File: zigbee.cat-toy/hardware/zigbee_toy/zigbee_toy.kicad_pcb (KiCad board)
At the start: 2 copper layers, 36 x 23 mm, 71 parts, among them J1 USB-C 16P, J3 LiPo 1S (JST-PH), J4 MOTOR, J5 SPEAKER, Q1 AO3401A, Q2 AO3400A, SW1 PAIR / BOOT, U1 ESP32-C6-MINI-1U-H4, U2 DRV8213DSGR, U3 LIS2DW12TR-MS, U4 TP4054-42-SOT25R, U5 XB5353A, U6 RT9080-33GJ5, U7 USBLC6-2SC6, Y1 32.768k 12.5pF

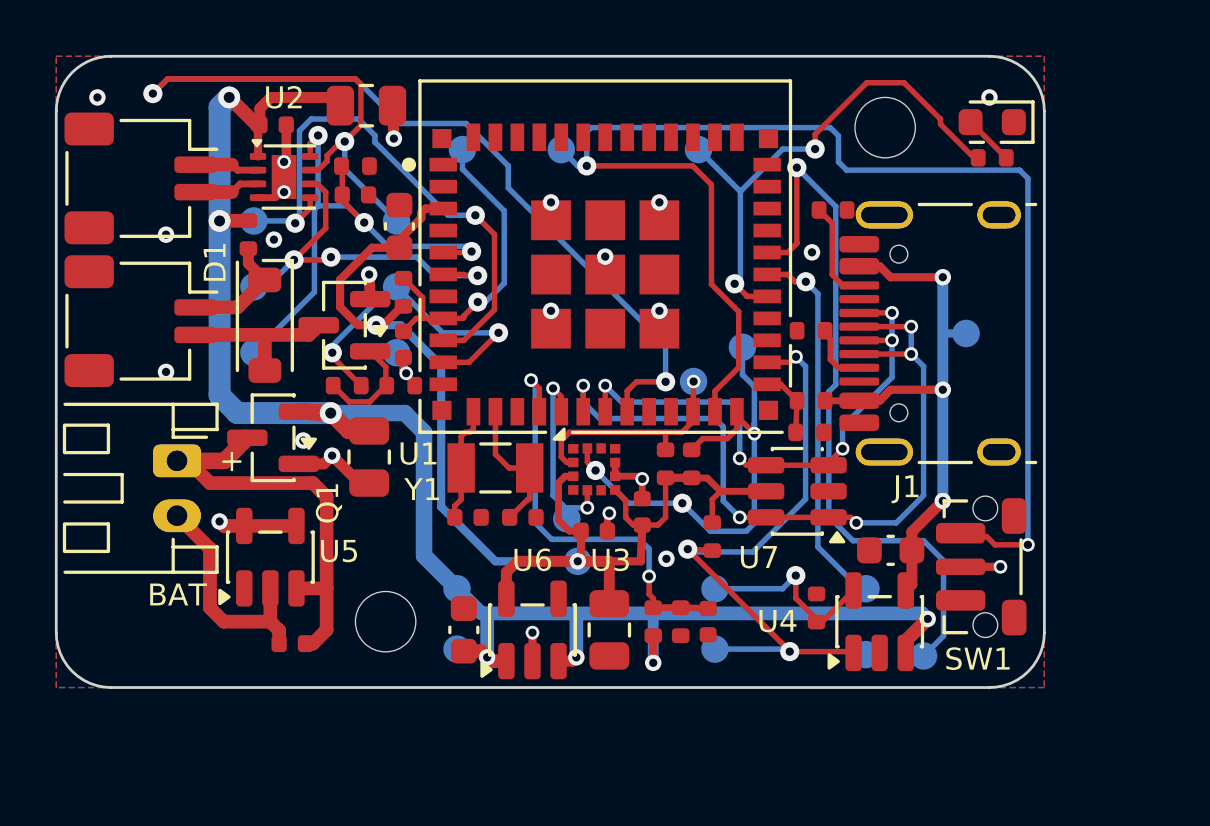
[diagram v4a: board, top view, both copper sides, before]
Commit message: zigbee.cat-toy: rev B review should-fix items
- C14 100 nF at module pin 3, beside C9. C2 moves 0.45 mm west to make
  room; the router's GAINSEL detour along the top edge is gone.
- R5 10 k pull-up on IO9 (BOOT). Its BTN via runs on the back to TP17,
  just below the antenna keepout; GAINSEL drops to a lane under it and
  TP21 (EN) moves down the EN route.
- Accelerometer pad 4 to GND, per the datasheet's connection column.
  ACC_INT1 now crosses under the sensor; TP13 moves onto its vertical.
- Two ground vias under the TP4054 on pin 2. The VBAT lane dips below
  them; TP20 and TP22 move off the charger's underside.
- gen_silk drops a pin-1 dot that lands on a neighbour's pad.

Co-Authored-By: Claude Opus 5.5 <noreply@anthropic.com>
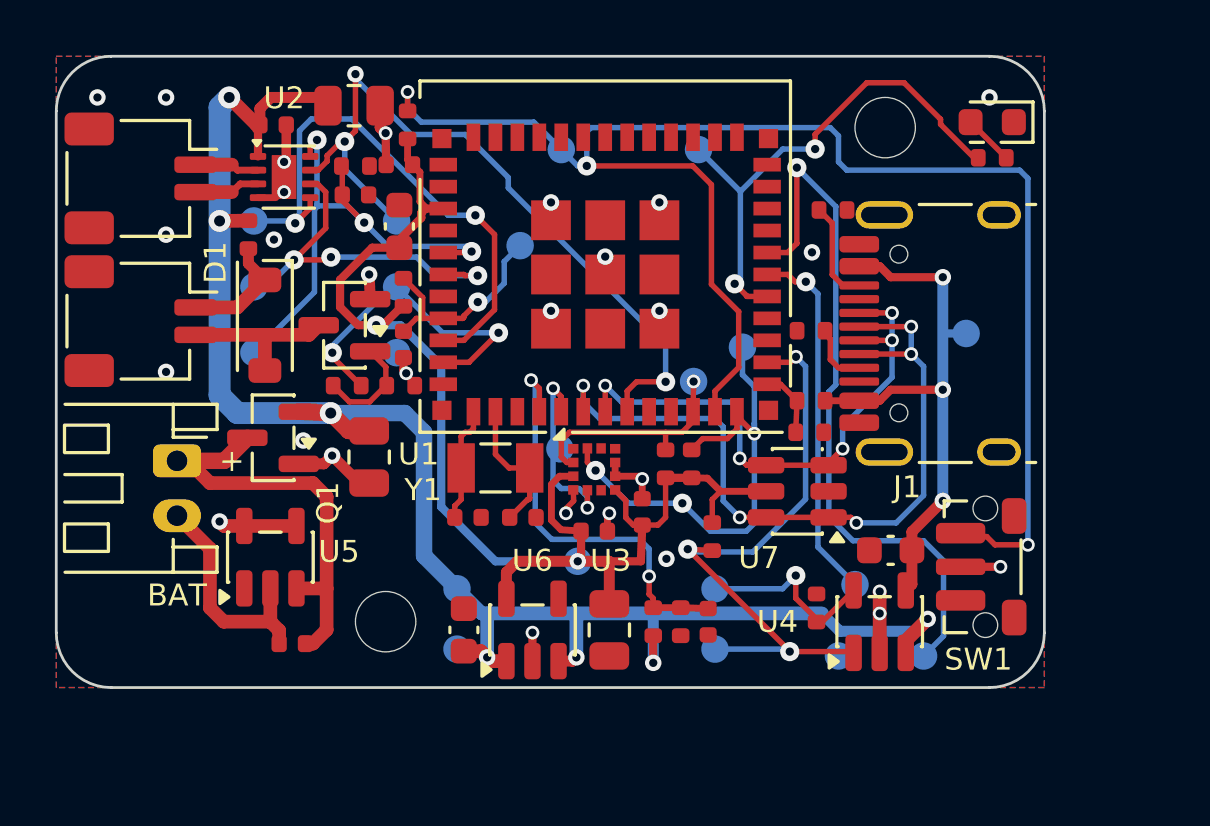
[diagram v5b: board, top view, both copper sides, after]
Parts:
- added C14: 100n, Capacitor_SMD:C_0402_1005Metric, F.Cu at (12.5, 3.95)
- added R5: 10k, Resistor_SMD:R_0402_1005Metric, F.Cu at (12.8, 2.50)
- moved TP21 4.08 mm to (16.9, 6.90)
- moved TP13 2.56 mm to (18.4, 14.3)
- moved TP22 1.00 mm to (28.5, 21.9)
- moved C2 0.45 mm to (10.8, 1.80)
- moved TP20 0.43 mm to (29.1, 19.2)
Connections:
- U3 pad 4: (no net) -> GND
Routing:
- net MOT_GAINSEL: track 42.7 -> 27.4 mm
- net BTN: track 49.2 -> 56.7 mm, vias 2 -> 3
- net GND: track 15.9 -> 20.2 mm, vias 24 -> 28
- net 3V3: track 45.7 -> 49.6 mm
- net EN: track 11.7 -> 7.78 mm

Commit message: zigbee.cat-toy: rev B placement pass (USB-C side, battery corner)
- CC pull-downs R1/R2 stand vertical in the channel between the module's
  right pads and the receptacle pads, one column, ground pads facing each
  other with a shared via. They were the only parts that belong there.
- VBUS divider R14/R15 moved out of that channel to the strip above the
  receptacle beside H1, fed from the upper VBUS pad A9. VBUS_SENSE comes
  back to pin 25 on the back layer under the module's right pad column.
  DBG_TX and DBG_RX vias moved to make room; CHG_STAT unchanged.
- Battery corner: U5 moved to 1.4 mm from the JST-PH housing (was 0.6),
  Q1 and C1 shifted right, C1 gets its own ground via, CELL_P goes round
  U5's ground pad on the far side. U5 and C15 stay 0.7 / 1.0 mm outside
  the 4 mm screw-head circle at H2 (a first try put them 0.3 mm from it).
- U7 (USBLC6) stays below the receptacle. The channel beside the data
  pads is 2.1 mm wide between the module pads and the receptacle pads;
  the SOT-23-6 needs 3.6 mm across or 2.5 mm turned, so it cannot sit
  closer without moving the module or the connector. The 5 mm stub is
  fine at USB full speed.
- U1 silk reference moved below the module's corner, standing between C1
  and the crystal. README layout notes and both renders regenerated.
- Review doc: status line, every item from the datasheet review applied.

DRC: courtyard warnings only, 0 unconnected. check_spacing 0.21 mm.
JLC export: 49 placements fit.

Co-Authored-By: Claude Fable 5.1 <noreply@anthropic.com>
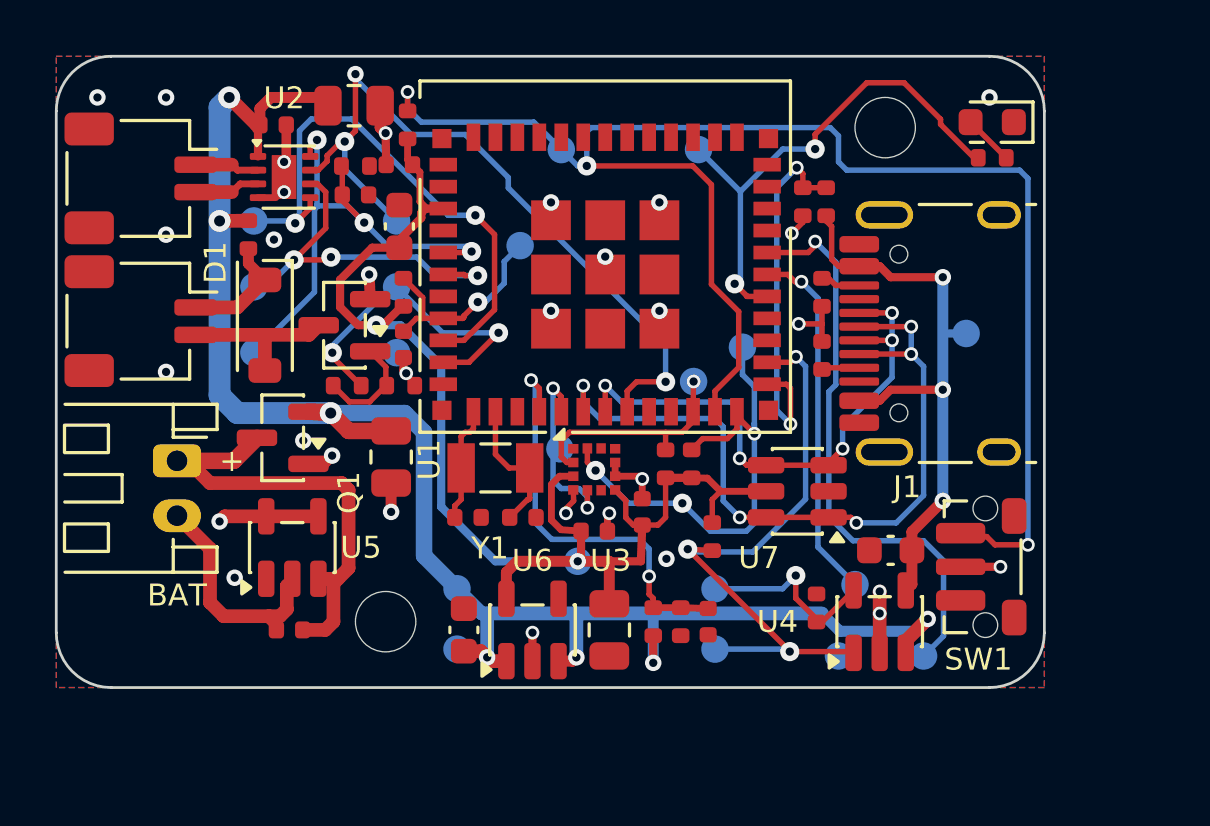
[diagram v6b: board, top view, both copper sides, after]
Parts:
- moved R15 8.40 mm to (27.2, 5.30), turned to -90 degrees
- moved R14 7.27 mm to (28.1, 5.30), turned to 90 degrees
- moved R2 3.03 mm to (27.9, 8.60), turned to -90 degrees
- moved R1 0.98 mm to (27.9, 10.9), turned to 90 degrees
- moved U5 0.87 mm to (8.60, 17.9)
- moved C1 0.80 mm to (12.2, 14.6)
- moved C15 0.51 mm to (8.50, 20.9)
- moved Q1 0.35 mm to (8.25, 13.9)
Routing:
- net VBUS_SENSE: track 2.49 -> 13.7 mm, vias 0 -> 2
- net DBG_TX: track 26.0 -> 21.1 mm
- net GND: track 20.2 -> 22.9 mm, vias 28 -> 31
- net CC2: track 3.70 -> 1.46 mm
- net VBUS: track 20.5 -> 22.0 mm
- net CELL_P: track 15.8 -> 16.9 mm
- net CC1: track 2.31 -> 1.38 mm
